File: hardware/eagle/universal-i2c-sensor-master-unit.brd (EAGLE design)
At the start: 53.3 x 74.3 mm, 30 parts, among them X1 22-23-2041, X10 22-23-2041, X11 22-23-2041, X12 22-23-2021, X13 22-23-2021, X14 22-23-2021, X2 22-23-2041, X3 22-23-2041, X4 22-23-2041, X5 22-23-2041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

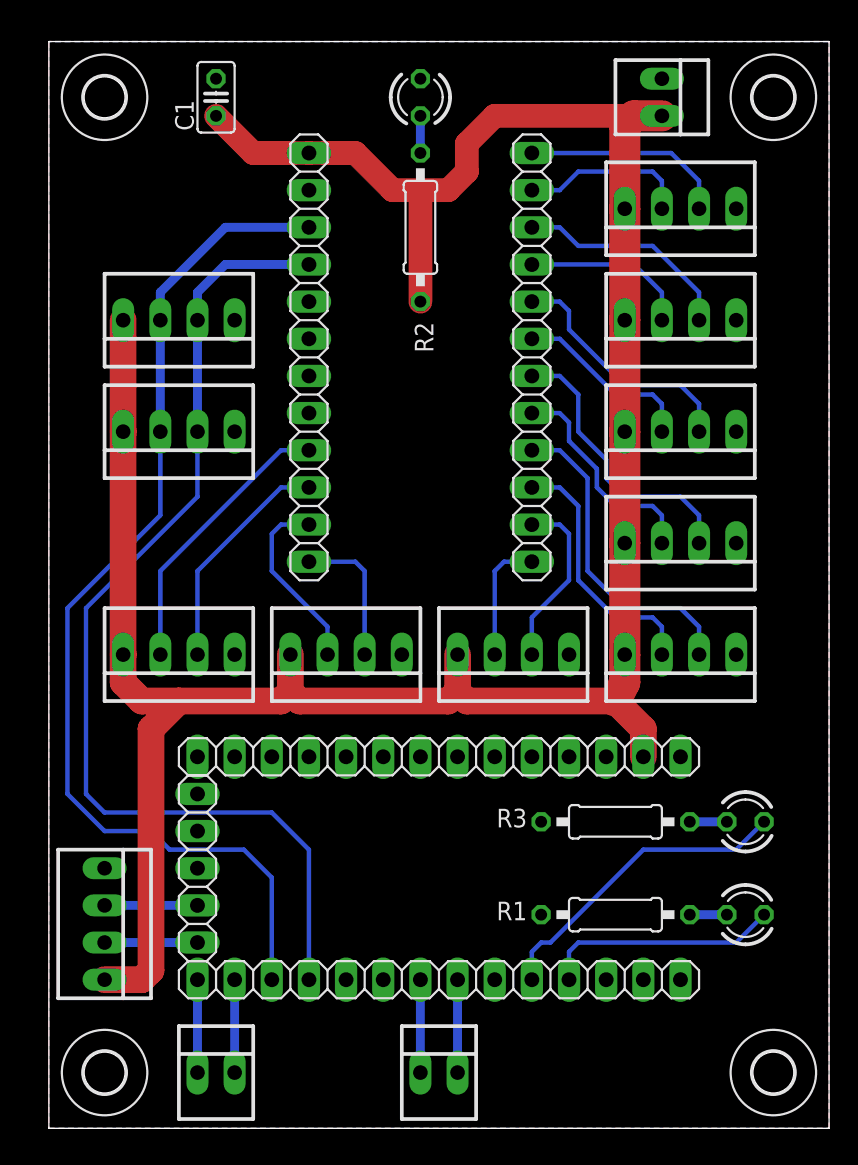
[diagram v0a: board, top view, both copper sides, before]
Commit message: Layout Reworked & Lables
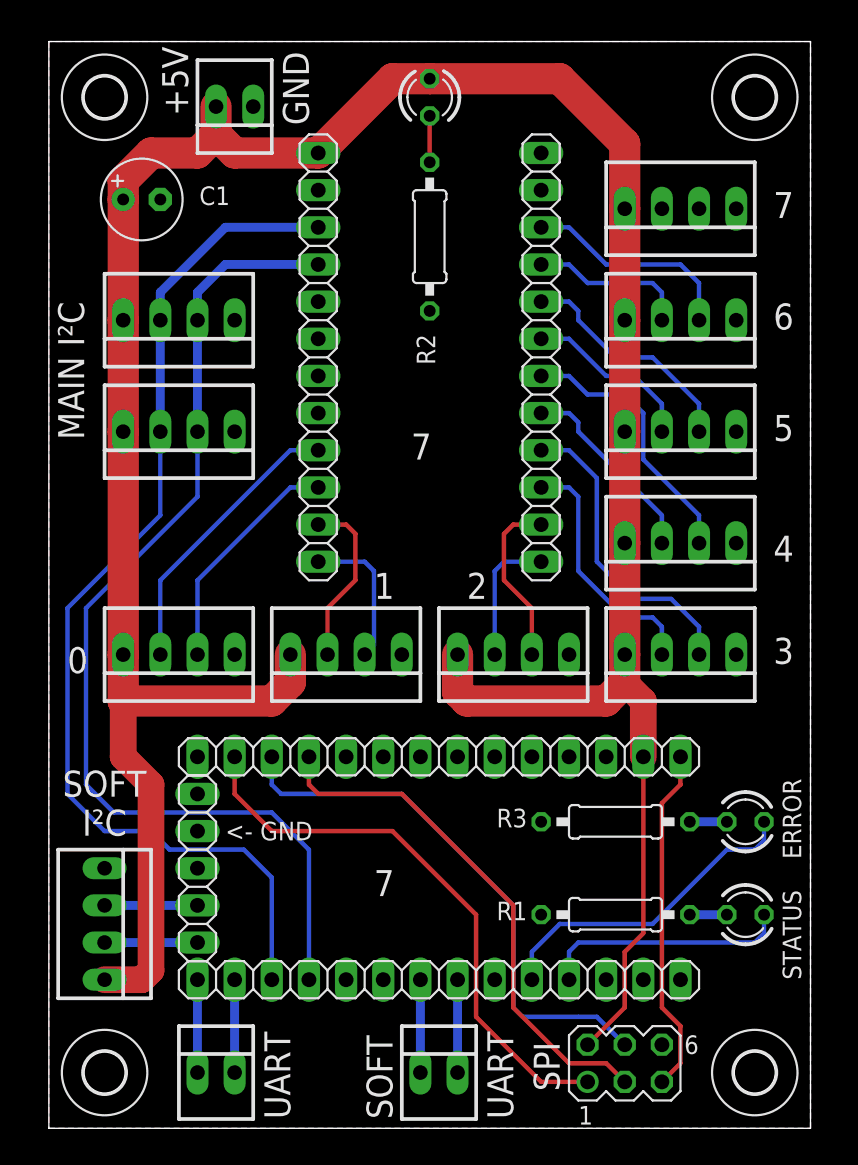
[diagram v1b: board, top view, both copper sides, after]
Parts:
- added SV1: (no value), con-lstb:MA03-2
- C1: device rcl:C025-025X050 -> rcl:E2,5-6
- moved X12 29.2 mm to (12.7, 69.8), turned to 180 degrees
- moved C1 8.64 mm to (6.35, 63.5), turned to 0 degrees
- moved H1 1.27 mm to (48.3, 3.81)
- moved H3 1.27 mm to (48.3, 70.5)
- moved R2 0.90 mm to (26.0, 61.0), turned to 90 degrees
- moved POWER-LED 0.64 mm to (26.0, 70.5), turned to 270 degrees
- moved JP3 0.63 mm to (33.7, 52.7)
- moved JP4 0.63 mm to (18.4, 52.7)
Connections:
- removed net MIS0: JP1.13
- removed net RST2: JP1.1
- new net MISO: JP1.13, SV1.1
- new net RST: JP1.1, SV1.5
- net +5V: now also C1.+, POWER-LED.A, SV1.2; no longer C1.1, R2.2
- net GND: now also C1.-, R2.1, SV1.6; no longer C1.2, POWER-LED.K
- net MOSI: now also SV1.4
- net N$2: now also POWER-LED.K, R2.2; no longer POWER-LED.A, R2.1
- net SCK: now also SV1.3
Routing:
- net MISO: track 0.00 -> 38.9 mm
- net MOSI: track 0.00 -> 37.5 mm
- net SCK: track 0.00 -> 36.0 mm
- net RST: track 0.00 -> 23.8 mm
- net +5V: track 178.1 -> 192.5 mm
- net SC7: track 14.1 -> 0.00 mm
- net SD7: track 11.6 -> 0.00 mm
- net SD4: track 15.2 -> 13.4 mm
- net SC5: track 17.0 -> 16.0 mm
- net SC4: track 19.5 -> 18.5 mm
- net SC3: track 22.1 -> 21.0 mm
- net SD1: track 12.6 -> 11.8 mm
- net D13: track 16.3 -> 17.0 mm
- net D12: track 21.5 -> 22.2 mm
- net SDA: track 72.2 -> 72.9 mm
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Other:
- board size 53.3 x 74.3 mm -> 52.1 x 74.3 mm
- board text added: "+5V"
- board text added: "0"
- board text added: "1"
- board text added: "2"
- board text added: "3"
- board text added: "4"
- board text added: "5"
- board text added: "6"
- board text added: "7"
- board text added: "<- GND"
- board text added: "ERROR"
- board text added: "GND"
- board text added: "MAIN I²C"
- board text added: "SOFT"
- board text added: "SOFT I²C"
- board text added: "SPI"
- board text added: "STATUS"
- board text added: "UART"

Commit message: some fixes & more lables
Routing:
- net +5V: track 192.5 -> 204.6 mm
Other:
- board text added: "Adafruit ItsyBitsy 32u4"
- board text added: "Adafruit TCA9548A I²C MUX"
- board text added: "GND ->"
- board text added: "POWER"
- board text added: "Team Onestone © DA & JJM, 2019."
- board text added: "Universal I²C Sensor Master Unit HW-Ver. 1.0"
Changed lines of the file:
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@@
 <text x="17.78" y="68.58" size="1.778" layer="21" rot="R90">GND</text>
 <text x="9.525" y="69.215" size="1.778" layer="21" rot="R90">+5V</text>
-<text x="24.765" y="45.72" size="1.778" layer="21">7</text>
-<text x="22.225" y="15.875" size="1.778" layer="21">7</text>
-<text x="12.065" y="19.685" size="1.27" layer="21">&lt;- GND</text>
+<text x="24.13" y="17.78" size="1.143" layer="21" align="center">Adafruit
+ItsyBitsy 32u4 </text>
+<text x="12.065" y="19.685" size="1.016" layer="21">&lt;- GND</text>
 <text x="51.435" y="10.16" size="1.27" layer="21" rot="R90">STATUS</text>
 <text x="31.75" y="0.635" size="1.778" layer="21" rot="R90">UART</text>
 <text x="51.435" y="18.415" size="1.27" layer="21" rot="R90">ERROR</text>
+<text x="26.035" y="45.085" size="1.143" layer="21" align="center">Adafruit
+TCA9548A
+I²C MUX</text>
+<text x="16.51" y="64.77" size="1.016" layer="21" rot="R180">GND -&gt;</text>
+<text x="8.89" y="40.005" size="1.27" layer="21" align="center">Team Onestone
+© DA &amp; JJM, 2019.</text>
+<text x="38.1" y="71.12" size="1.016" layer="21" align="center">Universal I²C Sensor
+Master Unit
+HW-Ver. 1.0</text>
+<text x="23.495" y="66.675" size="1.27" layer="21" rot="R90">POWER</text>
+<text x="26.035" y="49.53" size="0.889" layer="16" font="vector" rot="MR0" align="center">Team Onestone
+© DA &amp; JJM, 2019.</text>
+<text x="38.1" y="71.12" size="0.889" layer="16" font="vector" rot="MR180" align="center">Universal I²C Sensor
+Master Unit
+HW-Ver. 1.0</text>
 </plain>
 <attributes>
@@
 </element>
 <element name="C1" library="rcl" library_urn="urn:adsk.eagle:library:334" package="E2,5-6" package3d_urn="urn:adsk.eagle:package:23349/1" value="" x="6.35" y="63.5" smashed="yes">
-<attribute name="NAME" x="10.287" y="63.119" size="1.27" layer="25" ratio="10"/>
+<attribute name="NAME" x="2.921" y="62.357" size="1.27" layer="25" ratio="10" rot="R90"/>
 <attribute name="SPICEPREFIX" value="C" x="6.35" y="63.5" size="1.778" layer="27" display="off"/>
 <attribute name="VALUE" x="9.017" y="60.833" size="1.27" layer="27" ratio="10"/>
@@
 <wire x1="39.37" y1="67.31" x2="39.37" y2="62.865" width="2.1336" layer="1"/>
 <wire x1="39.37" y1="32.385" x2="39.37" y2="30.48" width="2.1336" layer="1"/>
-<wire x1="39.37" y1="30.48" x2="38.1" y2="29.21" width="2.1336" layer="1"/>
-<wire x1="28.575" y1="29.21" x2="27.94" y2="29.845" width="2.1336" layer="1"/>
-<wire x1="27.94" y1="29.845" x2="27.94" y2="32.385" width="2.1336" layer="1"/>
-<wire x1="38.1" y1="29.21" x2="28.575" y2="29.21" width="2.1336" layer="1"/>
+<wire x1="38.1" y1="29.21" x2="39.37" y2="30.48" width="2.1336" layer="1"/>
 <wire x1="6.985" y1="10.795" x2="6.985" y2="23.495" width="1.8288" layer="1"/>
 <wire x1="6.985" y1="23.495" x2="5.08" y2="25.4" width="1.8288" layer="1"/>
@@
 <wire x1="26.035" y1="71.755" x2="34.925" y2="71.755" width="2.1336" layer="1"/>
 <wire x1="34.925" y1="71.755" x2="39.37" y2="67.31" width="2.1336" layer="1"/>
+<wire x1="16.51" y1="30.48" x2="17.78" y2="29.21" width="2.1336" layer="1"/>
+<wire x1="17.78" y1="29.21" x2="26.67" y2="29.21" width="2.1336" layer="1"/>
+<wire x1="26.67" y1="29.21" x2="27.94" y2="30.48" width="2.1336" layer="1"/>
+<wire x1="27.94" y1="30.48" x2="27.94" y2="32.385" width="2.1336" layer="1"/>
+<wire x1="27.94" y1="30.48" x2="29.21" y2="29.21" width="2.1336" layer="1"/>
+<wire x1="29.21" y1="29.21" x2="38.1" y2="29.21" width="2.1336" layer="1"/>
 </signal>
 <signal name="SDA">

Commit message: Add files via upload
SC7 und SD7 angeschlossen
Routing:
- net SC7: track 0.00 -> 14.2 mm
- net SD7: track 0.00 -> 13.1 mm
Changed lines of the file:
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@@
 <?xml version="1.0" encoding="utf-8"?>
 <!DOCTYPE eagle SYSTEM "eagle.dtd">
-<eagle version="9.3.1">
+<eagle version="9.3.2">
 <drawing>
 <settings>
@@
 <contactref element="JP3" pad="2"/>
 <contactref element="X7" pad="3"/>
-<wire x1="33.655" y1="64.135" x2="41.91" y2="62.865" width="0" layer="19" extent="1-1"/>
+<wire x1="41.91" y1="62.865" x2="41.91" y2="60.96" width="0.381" layer="16"/>
+<wire x1="41.91" y1="60.96" x2="41.275" y2="60.325" width="0.381" layer="16"/>
+<wire x1="38.1" y1="60.325" x2="36.83" y2="61.595" width="0.381" layer="16"/>
+<wire x1="36.83" y1="61.595" x2="36.83" y2="63.5" width="0.381" layer="16"/>
+<wire x1="36.83" y1="63.5" x2="36.195" y2="64.135" width="0.381" layer="16"/>
+<wire x1="36.195" y1="64.135" x2="33.655" y2="64.135" width="0.381" layer="16"/>
+<wire x1="41.275" y1="60.325" x2="38.1" y2="60.325" width="0.381" layer="16"/>
 </signal>
 <signal name="SC6">
@@
 <contactref element="JP3" pad="1"/>
 <contactref element="X7" pad="2"/>
-<wire x1="33.655" y1="66.675" x2="44.45" y2="62.865" width="0" layer="19" extent="1-1"/>
+<wire x1="33.655" y1="66.675" x2="43.815" y2="66.675" width="0.381" layer="16"/>
+<wire x1="43.815" y1="66.675" x2="44.45" y2="66.04" width="0.381" layer="16"/>
+<wire x1="44.45" y1="66.04" x2="44.45" y2="62.865" width="0.381" layer="16"/>
 </signal>
 <signal name="RST|M">

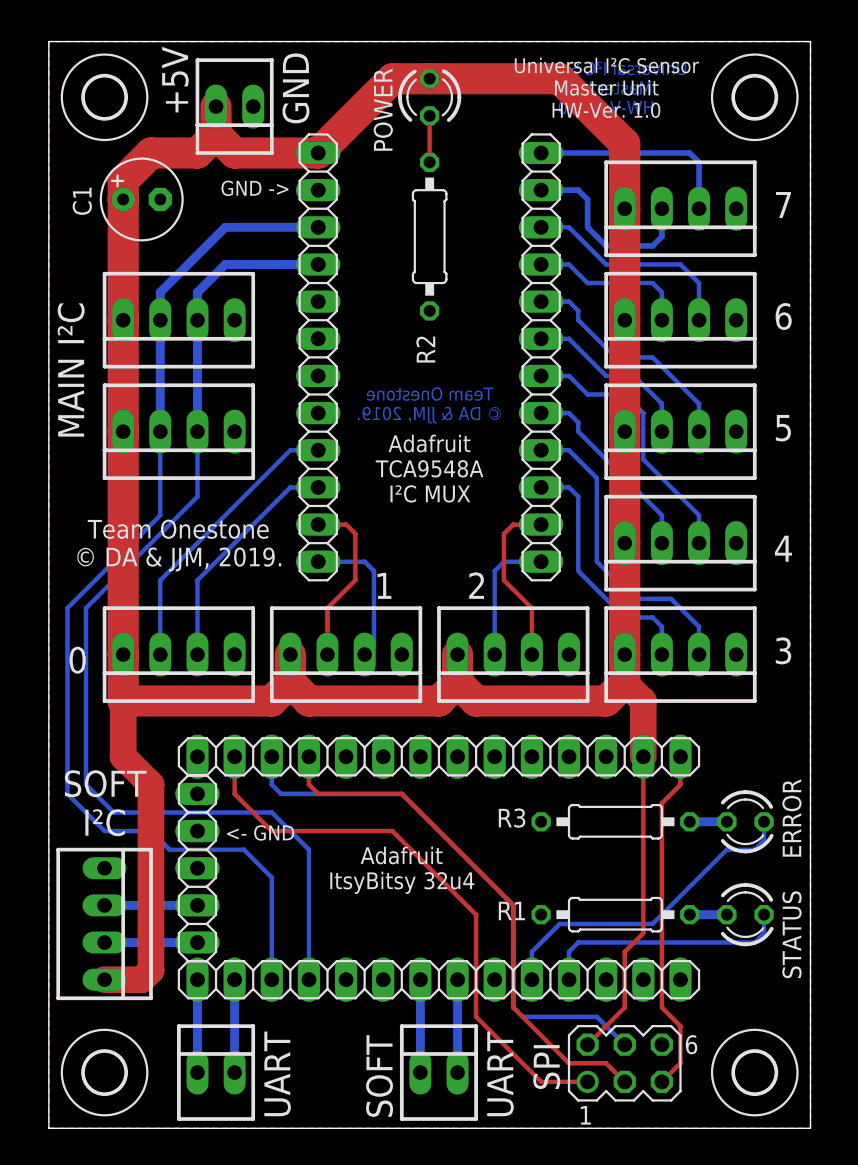
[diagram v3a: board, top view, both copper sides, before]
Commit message: SMD Jumper for Soft / Hard I2C
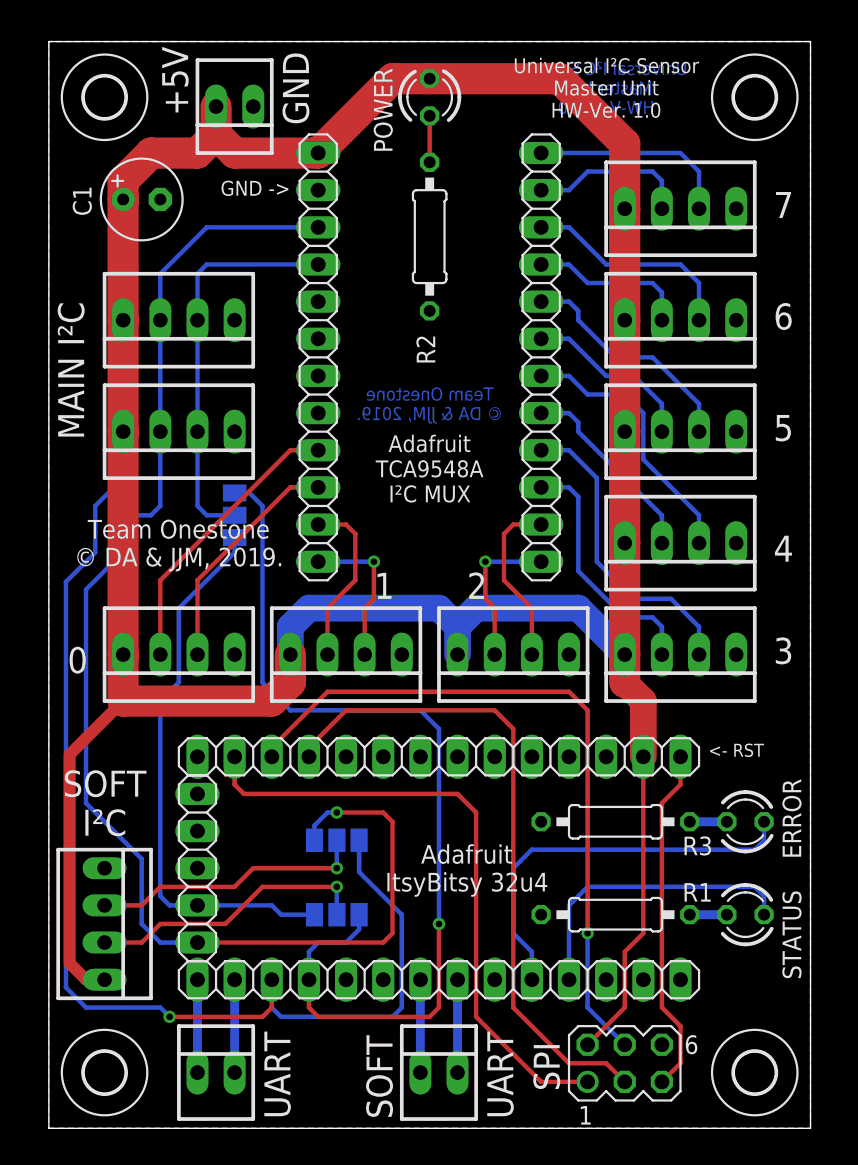
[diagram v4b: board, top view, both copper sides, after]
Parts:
- added SJ1, SJ2, SJ3, SJ4: (no value), jumper:SJ_2
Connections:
- new net SCL_EXTRA: SJ4.2, X11.3
- new net SCL_SENSORS: JP4.4, SJ2.2, X8.2, X9.2
- new net SDA_EXTRA: SJ3.2, X11.2
- new net SDA_SENSORS: JP4.3, SJ1.2, X8.3, X9.3
- net D4: now also SJ1.3, SJ3.3; no longer X11.3
- net D6: now also SJ2.3, SJ4.3; no longer X11.2
- net SCL: now also SJ2.1, SJ4.1; no longer JP4.4, X8.2, X9.2
- net SDA: now also SJ1.1, SJ3.1; no longer JP4.3, X8.3, X9.3
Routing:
- net D4: track 6.35 -> 61.6 mm, vias 0 -> 1
- net D6: track 6.35 -> 37.7 mm
- net SDA_SENSORS: track 0.00 -> 30.8 mm
- net SCL_SENSORS: track 0.00 -> 27.2 mm
- net SCL_EXTRA: track 0.00 -> 19.4 mm, vias 0 -> 1
- net SDA_EXTRA: track 0.00 -> 18.8 mm, vias 0 -> 1
- net MOSI: track 37.5 -> 48.2 mm, vias 0 -> 1
- net SCK: track 36.0 -> 45.0 mm
- net SCL: track 71.8 -> 65.1 mm, vias 0 -> 1
- net D12: track 22.2 -> 27.4 mm
- net SDA: track 72.9 -> 77.1 mm, vias 0 -> 1
- net MISO: track 38.9 -> 42.6 mm
- net D13: track 17.0 -> 20.5 mm
- net +5V: track 204.6 -> 207.0 mm
- net SD7: track 13.1 -> 10.9 mm
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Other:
- board text added: "<- RST"
- board text removed: "<- GND"
